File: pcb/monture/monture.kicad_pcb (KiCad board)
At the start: 2 copper layers, 150 x 110 mm, 32 parts, among them U1 Teensy 4.1

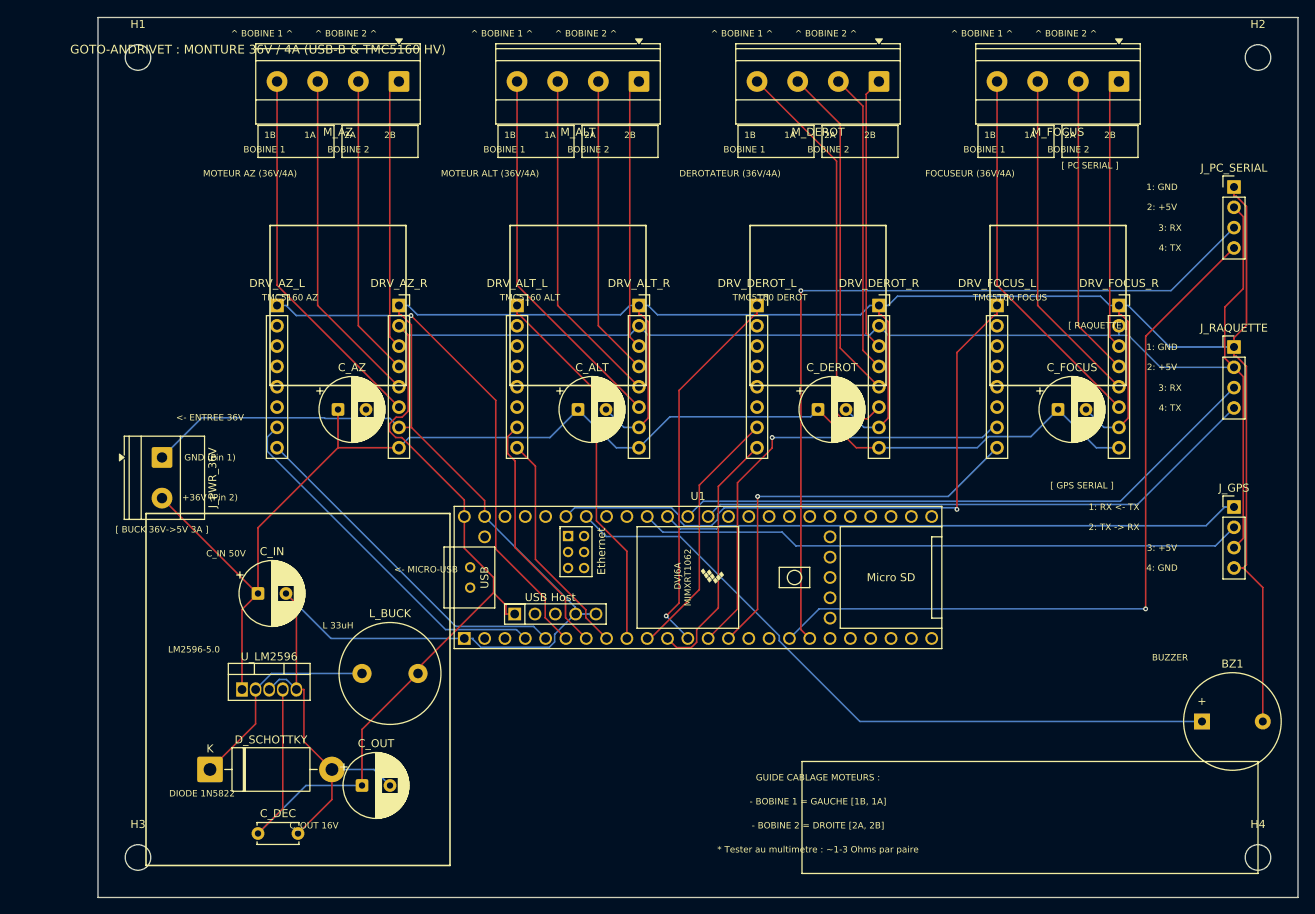
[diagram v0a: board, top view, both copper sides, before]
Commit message: Correction mécanique PCB/boîtiers : chanfreins 45°, DRC KiCad 0 erreur, recalibrage OpenSCAD/FreeCAD et firmware
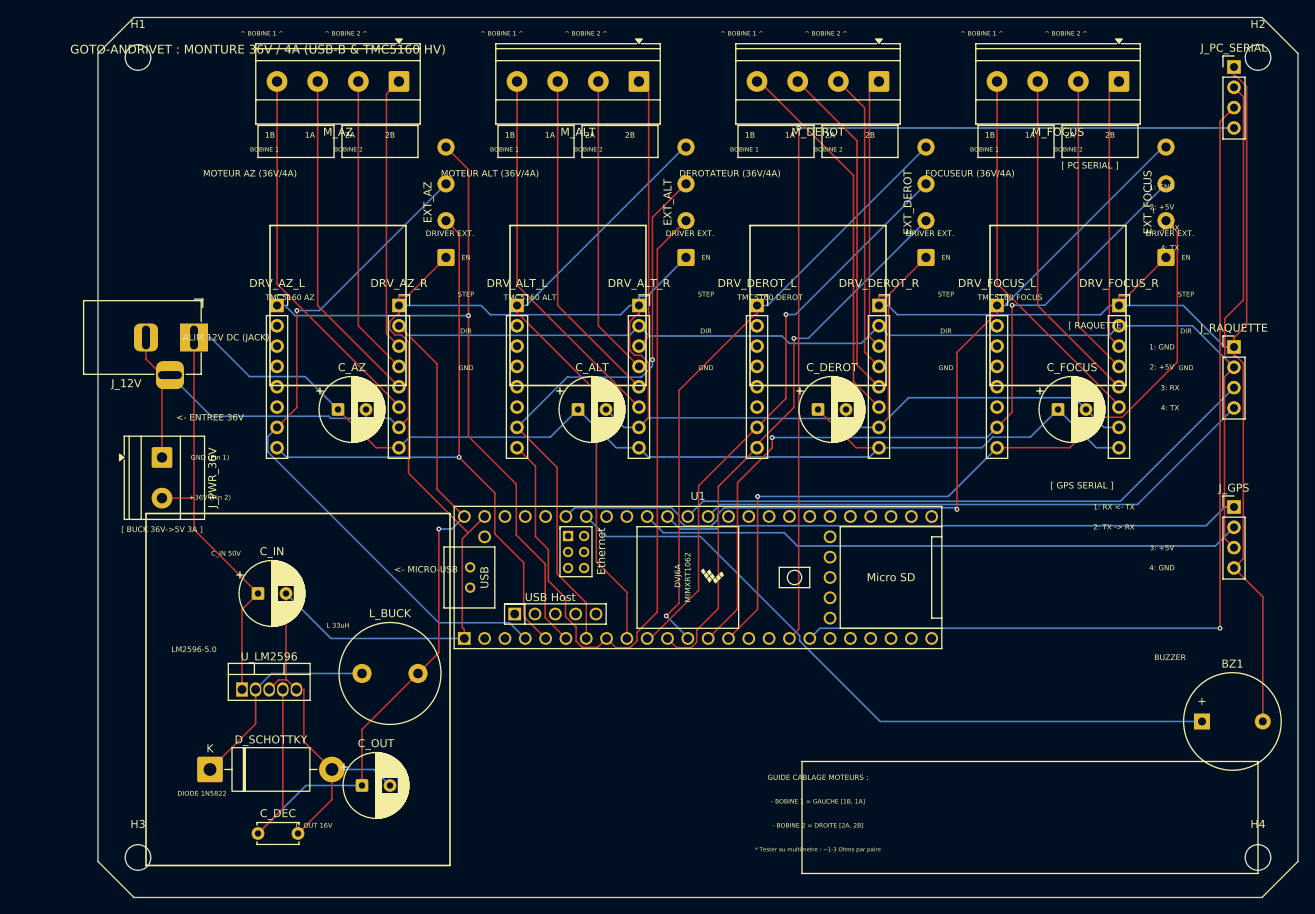
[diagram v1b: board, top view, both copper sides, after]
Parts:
- added EXT_ALT: Ext. Driver, SolderWire-0.5sqmm_1x04_P4.6mm_D0.9mm_OD2.1mm, F.Cu at (73.5, 30.0)
- added EXT_AZ: Ext. Driver, SolderWire-0.5sqmm_1x04_P4.6mm_D0.9mm_OD2.1mm, F.Cu at (43.5, 30.0)
- added EXT_DEROT: Ext. Driver, SolderWire-0.5sqmm_1x04_P4.6mm_D0.9mm_OD2.1mm, F.Cu at (103.5, 30.0)
- added EXT_FOCUS: Ext. Driver, SolderWire-0.5sqmm_1x04_P4.6mm_D0.9mm_OD2.1mm, F.Cu at (133.5, 30.0)
- added J_12V: 12V Jack, BarrelJack_Horizontal, F.Cu at (12.0, 40.0)
- moved J_PC_SERIAL 15.0 mm to (142.0, 6.19)
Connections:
- U1 pad 55: +5V -> (no net)
- U1 pad 56: USB_HOST_DM -> (no net)
- U1 pad 57: USB_HOST_DP -> (no net)
- U1 pad 58: GND -> (no net)
- U1 pad 59: GND -> (no net)
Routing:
- net ALT_DIR: track 28.5 -> 91.5 mm
- net GND: track 418.9 -> 476.6 mm
- net FOCUS_DIR: track 51.7 -> 96.9 mm
- net ALT_STEP: track 30.9 -> 74.6 mm, vias 0 -> 1
- net FOCUS_STEP: track 57.1 -> 98.6 mm, vias 1 -> 2
- net AZ_STEP: track 45.4 -> 86.2 mm, vias 0 -> 1
- net DEROT_STEP: track 32.3 -> 72.2 mm, vias 0 -> 1
- net DEROT_DIR: track 31.8 -> 70.0 mm, vias 0 -> 1
- net AZ_DIR: track 43.4 -> 80.6 mm, vias 0 -> 1
- net FOCUS_EN: track 79.8 -> 109.2 mm
- net DEROT_EN: track 47.6 -> 76.9 mm
- net ALT_EN: track 47.5 -> 76.8 mm
- net AZ_EN: track 65.6 -> 92.2 mm
- net +36V: track 166.4 -> 191.9 mm
- net PC_TX: track 95.7 -> 118.7 mm
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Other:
- outline, holes or cut-outs redrawn
- board text added: "ALIM 12V DC (JACK)"
- board text added: "DIR"
- board text added: "DRIVER EXT."
- board text added: "EN"
- board text added: "GND"
- board text added: "STEP"
